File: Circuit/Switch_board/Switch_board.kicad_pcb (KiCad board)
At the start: 2 copper layers, 50.8 x 31.7 mm, 31 parts, among them J1 switch_mode, J2 switch, P1 XT30, Q1 2N7002, Q2 2N7002, Q3 2N7002, Q4 2N7002, U1 DRV5023

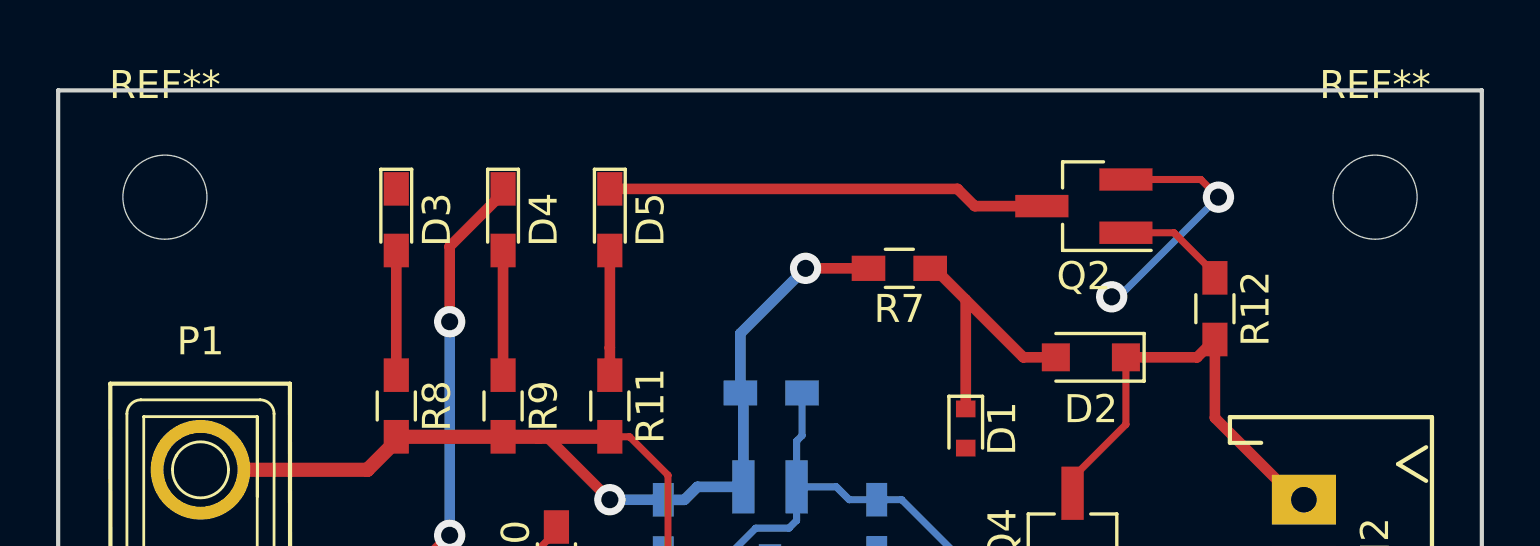
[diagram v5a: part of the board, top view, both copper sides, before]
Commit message: add silkskin description into Switch_board pcb
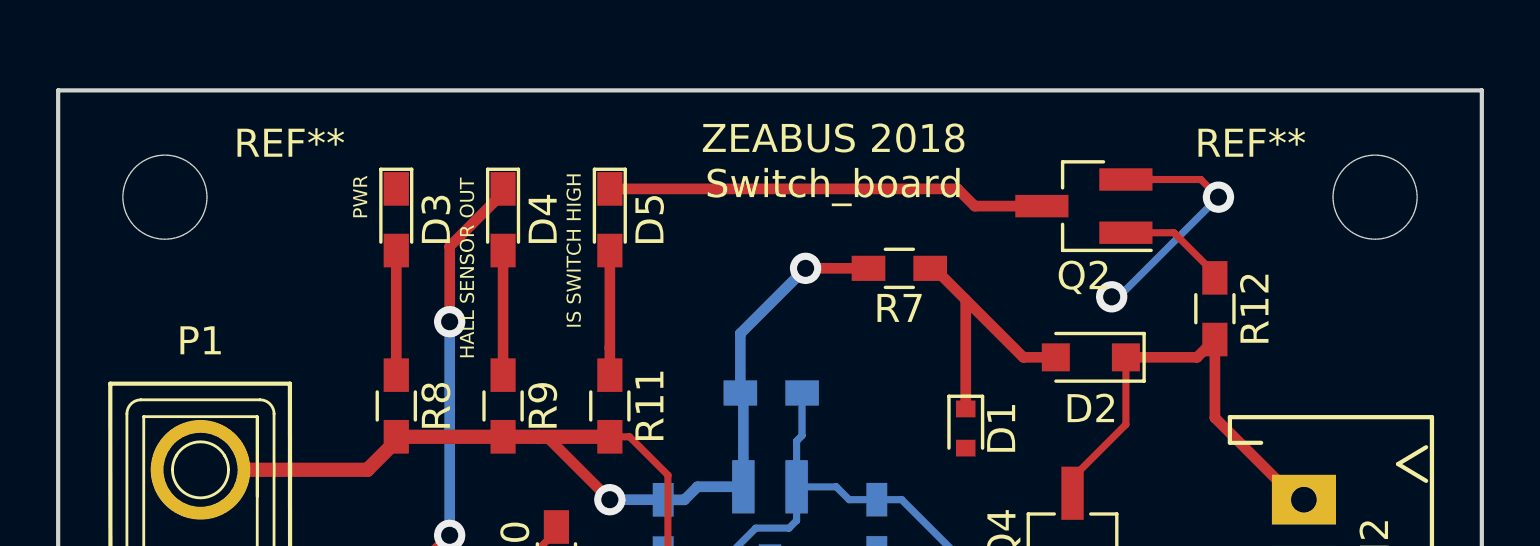
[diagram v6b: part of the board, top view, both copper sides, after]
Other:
- board text added: "HALL SENSOR OUT"
- board text added: "IS SWITCH HIGH"
- board text added: "NO.________ Note______________________________"
- board text added: "PWR"
- board text added: "ZEABUS 2018 Switch_board"
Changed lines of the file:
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@@
     (links 44)
     (no_connects 0)
-    (area 136.041714 103.668142 194.158286 141.019)
+    (area 139.624999 107.874999 190.575001 139.775001)
     (thickness 1.6)
-    (drawings 4)
+    (drawings 11)
     (tracks 118)
     (zones 0)
@@
   (page A4)
   (layers
-    (0 F.Cu signal)
-    (31 B.Cu signal)
+    (0 F.Cu signal hide)
+    (31 B.Cu signal hide)
     (32 B.Adhes user)
-    (33 F.Adhes user)
+    (33 F.Adhes user hide)
     (34 B.Paste user)
     (35 F.Paste user)
@@
     (pad_to_mask_clearance 0.2)
     (aux_axis_origin 0 0)
-    (visible_elements FFFFEF7F)
+    (visible_elements FFFFFF7F)
     (pcbplotparams
       (layerselection 0x00030_80000001)
@@
     (tags "mounting hole 3mm no annular")
     (attr virtual)
-    (fp_text reference REF** (at 0 -4) (layer F.SilkS)
+    (fp_text reference REF** (at 4.445 -1.905) (layer F.SilkS)
       (effects (font (size 1 1) (thickness 0.15)))
     )
@@
     (tags "mounting hole 3mm no annular")
     (attr virtual)
-    (fp_text reference REF** (at 0 -4) (layer F.SilkS)
+    (fp_text reference REF** (at -4.445 -1.905) (layer F.SilkS)
       (effects (font (size 1 1) (thickness 0.15)))
     )
@@
     (pad 1 np_thru_hole circle (at 0 0) (size 3 3) (drill 3) (layers *.Cu *.Mask))
   )
+  (gr_text "IS SWITCH HIGH" (at 158.115 113.665 90) (layer F.SilkS)
+    (effects (font (size 0.5 0.5) (thickness 0.125)))
+  )
+  (gr_text "HALL SENSOR OUT" (at 154.305 114.3 90) (layer F.SilkS)
+    (effects (font (size 0.5 0.5) (thickness 0.125)))
+  )
+  (gr_text PWR (at 150.495 111.76 90) (layer F.SilkS)
+    (effects (font (size 0.5 0.5) (thickness 0.125)))
+  )
+  (gr_text "NO.________ Note______________________________" (at 165.354 114.046) (layer B.SilkS)
+    (effects (font (size 1 1) (thickness 0.25)) (justify mirror))
+  )
+  (gr_text "ZEABUS 2018\nSwitch_board" (at 167.386 110.49) (layer F.SilkS)
+    (effects (font (size 1 1) (thickness 0.25)))
+  )
+  (dimension 31.75 (width 0.3) (layer Eco2.User)
+    (gr_text "31.750 mm" (at 198.2 123.825 270) (layer Eco2.User)
+      (effects (font (size 1.5 1.5) (thickness 0.3)))
+    )
+    (feature1 (pts (xy 190.5 139.7) (xy 199.55 139.7)))
+    (feature2 (pts (xy 190.5 107.95) (xy 199.55 107.95)))
+    (crossbar (pts (xy 196.85 107.95) (xy 196.85 139.7)))
+    (arrow1a (pts (xy 196.85 139.7) (xy 196.263579 138.573496)))
+    (arrow1b (pts (xy 196.85 139.7) (xy 197.436421 138.573496)))
+    (arrow2a (pts (xy 196.85 107.95) (xy 196.263579 109.076504)))
+    (arrow2b (pts (xy 196.85 107.95) (xy 197.436421 109.076504)))
+  )
+  (dimension 50.8 (width 0.3) (layer Eco2.User)
+    (gr_text "50.800 mm" (at 165.1 147.4) (layer Eco2.User)
+      (effects (font (size 1.5 1.5) (thickness 0.3)))
+    )
+    (feature1 (pts (xy 139.7 139.7) (xy 139.7 148.75)))
+    (feature2 (pts (xy 190.5 139.7) (xy 190.5 148.75)))
+    (crossbar (pts (xy 190.5 146.05) (xy 139.7 146.05)))
+    (arrow1a (pts (xy 139.7 146.05) (xy 140.826504 145.463579)))
+    (arrow1b (pts (xy 139.7 146.05) (xy 140.826504 146.636421)))
+    (arrow2a (pts (xy 190.5 146.05) (xy 189.373496 145.463579)))
+    (arrow2b (pts (xy 190.5 146.05) (xy 189.373496 146.636421)))
+  )
   (gr_line (start 139.7 107.95) (end 139.7 139.7) (layer Edge.Cuts) (width 0.15))

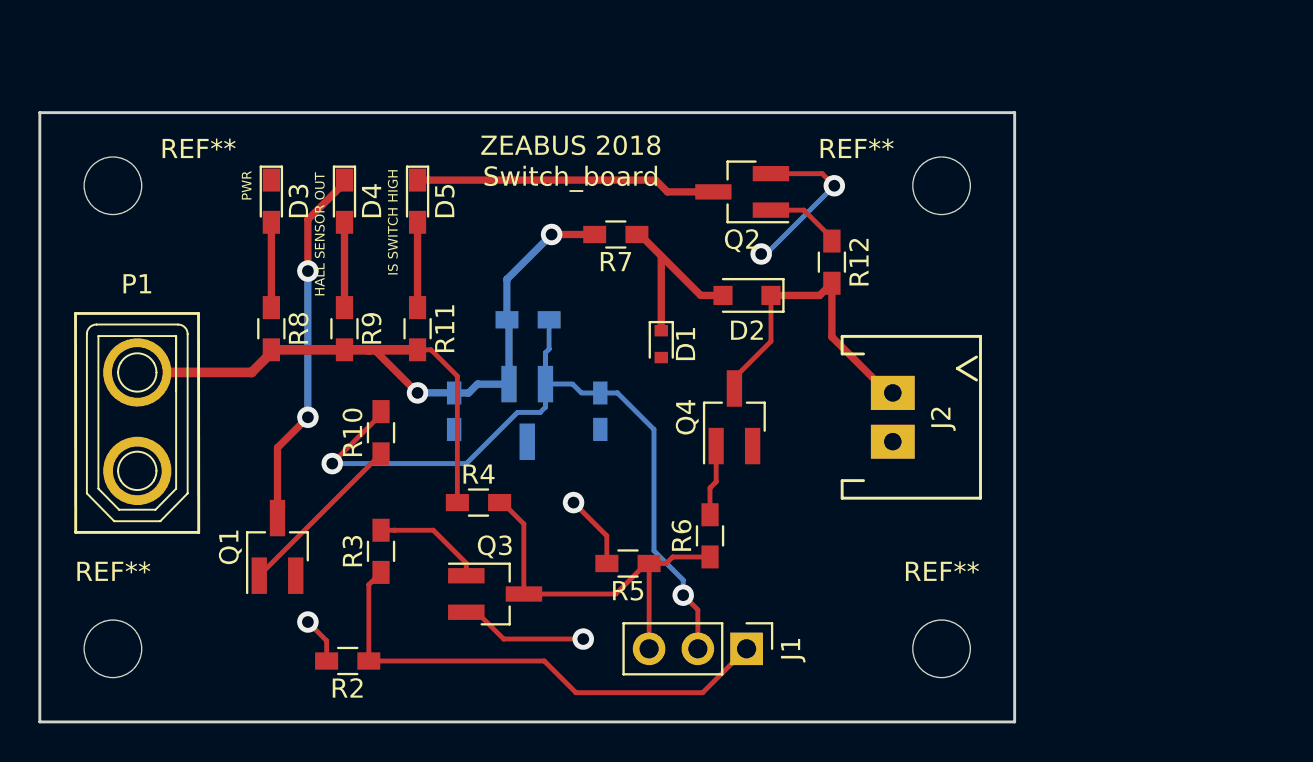
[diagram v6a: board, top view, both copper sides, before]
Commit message: added silkskin for connectors on Switch_board
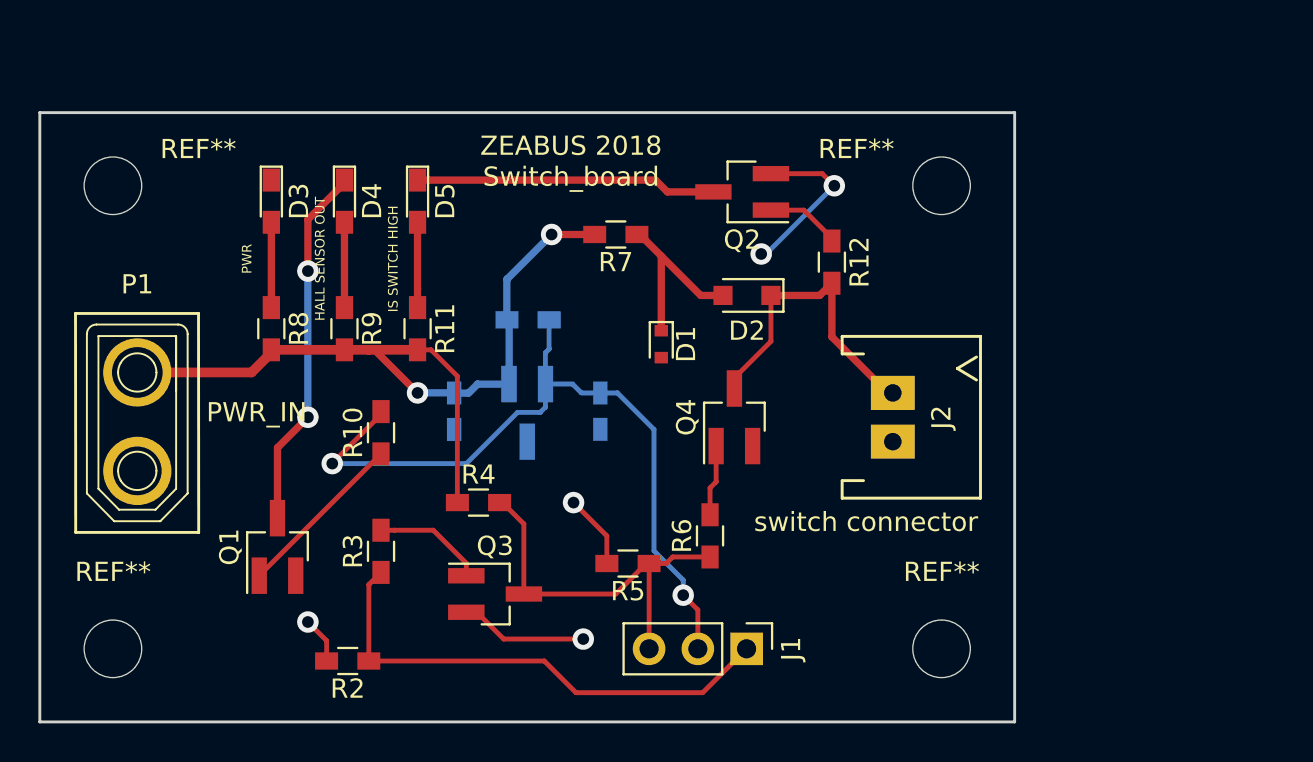
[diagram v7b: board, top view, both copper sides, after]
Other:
- board text added: "PWR_IN"
- board text added: "switch connector"
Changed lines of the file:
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@@
     (area 139.624999 107.874999 190.575001 139.775001)
     (thickness 1.6)
-    (drawings 11)
+    (drawings 13)
     (tracks 118)
     (zones 0)
@@
     (31 B.Cu signal hide)
     (32 B.Adhes user)
-    (33 F.Adhes user hide)
+    (33 F.Adhes user)
     (34 B.Paste user)
     (35 F.Paste user)
@@
       (outputformat 1)
       (mirror false)
-      (drillshape 1)
+      (drillshape 0)
       (scaleselection 1)
       (outputdirectory ""))
@@
     (pad 1 np_thru_hole circle (at 0 0) (size 3 3) (drill 3) (layers *.Cu *.Mask))
   )
-  (gr_text "IS SWITCH HIGH" (at 158.115 113.665 90) (layer F.SilkS)
+  (gr_text "switch connector" (at 182.753 129.286) (layer F.SilkS)
+    (effects (font (size 1 1) (thickness 0.25)))
+  )
+  (gr_text PWR_IN (at 151.003 123.571) (layer F.SilkS)
+    (effects (font (size 1 1) (thickness 0.25)))
+  )
+  (gr_text "IS SWITCH HIGH" (at 158.115 115.57 90) (layer F.SilkS)
     (effects (font (size 0.5 0.5) (thickness 0.125)))
   )
-  (gr_text "HALL SENSOR OUT" (at 154.305 114.3 90) (layer F.SilkS)
+  (gr_text "HALL SENSOR OUT" (at 154.305 115.57 90) (layer F.SilkS)
     (effects (font (size 0.5 0.5) (thickness 0.125)))
   )
-  (gr_text PWR (at 150.495 111.76 90) (layer F.SilkS)
+  (gr_text PWR (at 150.495 115.57 90) (layer F.SilkS)
     (effects (font (size 0.5 0.5) (thickness 0.125)))
   )

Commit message: added silkskin description of magnetic pole for activate hall sensor
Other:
- board text added: "***FACE TOWARD SOUTH POLE***"
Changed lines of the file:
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@@
     (area 139.624999 107.874999 190.575001 139.775001)
     (thickness 1.6)
-    (drawings 13)
+    (drawings 14)
     (tracks 118)
     (zones 0)
@@
     (pad 1 np_thru_hole circle (at 0 0) (size 3 3) (drill 3) (layers *.Cu *.Mask))
   )
+  (gr_text "***FACE TOWARD SOUTH POLE***" (at 165.1 130.175) (layer B.SilkS)
+    (effects (font (size 1 1) (thickness 0.25)) (justify mirror))
+  )
   (gr_text "switch connector" (at 182.753 129.286) (layer F.SilkS)
